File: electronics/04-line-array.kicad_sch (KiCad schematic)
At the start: 54 parts, among them Q401 AO3400A, Q402 AO3400A, U401 ITR8307/S17/TR8, U402 ITR8307/S17/TR8, U403 ITR8307/S17/TR8, U404 ITR8307/S17/TR8, U405 ITR8307/S17/TR8, U406 ITR8307/S17/TR8, U407 ITR8307/S17/TR8, U408 ITR8307/S17/TR8, U409 ITR8307/S17/TR8, U410 ITR8307/S17/TR8, U411 ITR8307/S17/TR8, U412 ITR8307/S17/TR8

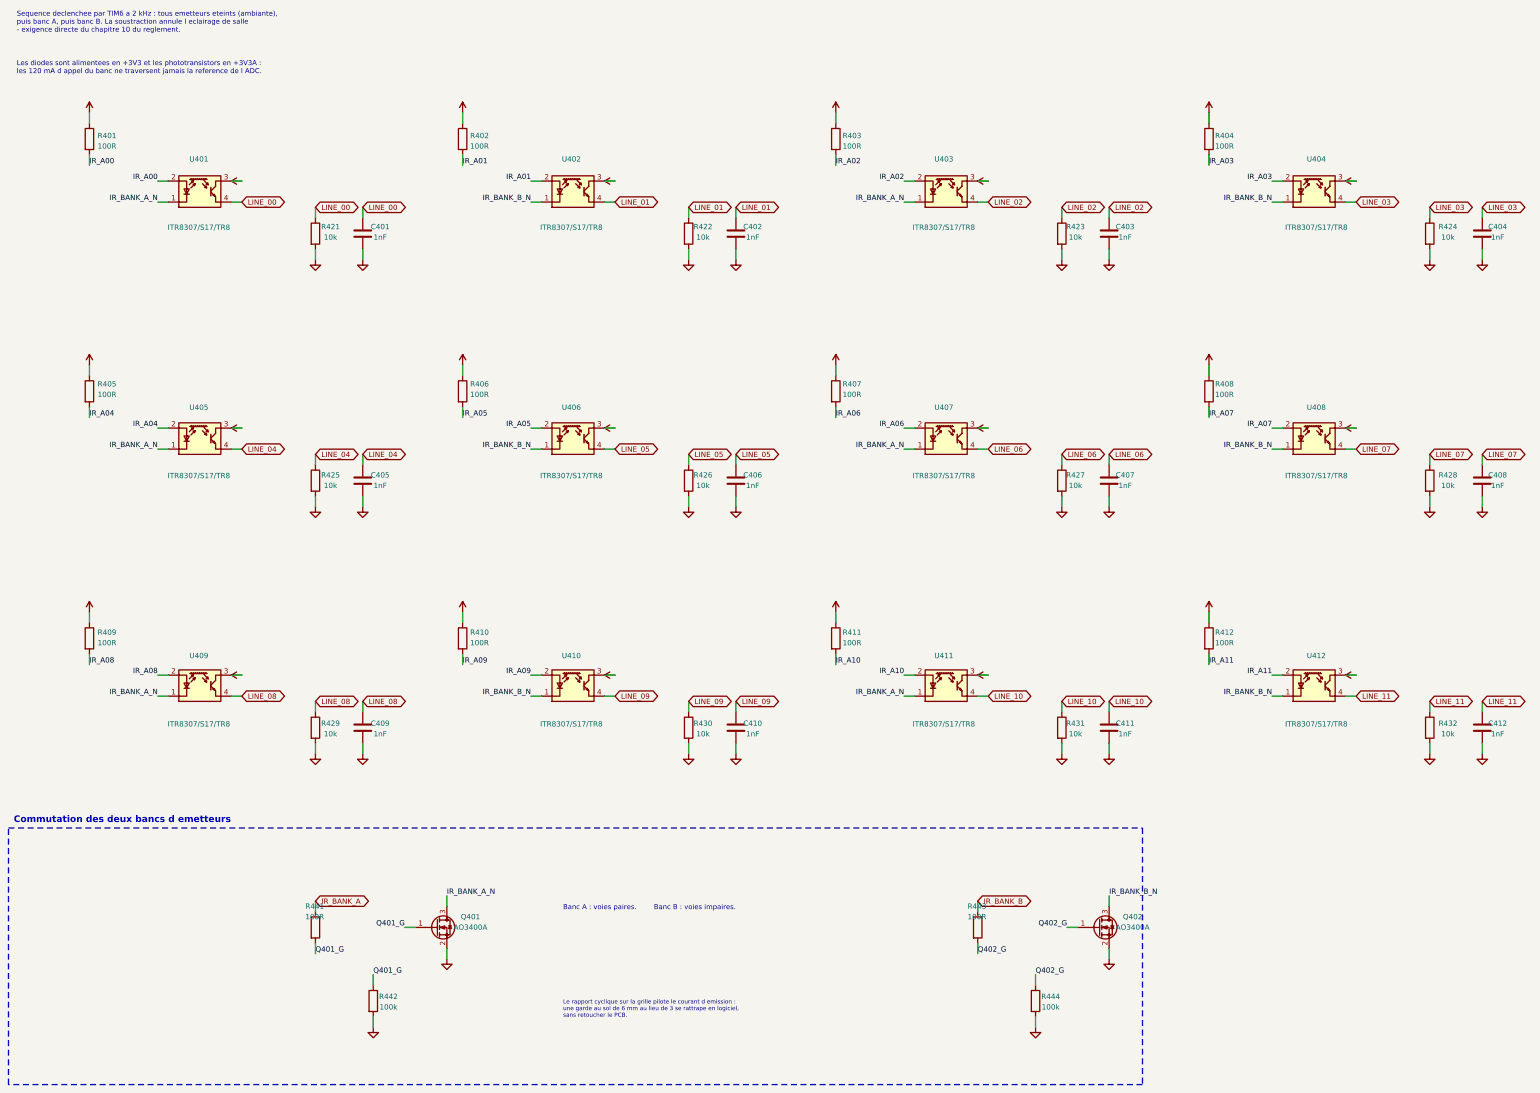
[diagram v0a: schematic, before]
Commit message: Passe le microcontrôleur en LQFP144 et lit les deux courants au même instant
Le LQFP100 avait ses seize entrées ADC prises — douze voies de ligne, trois
de télémétrie, une sortie de multiplexeur — et c'est ce multiplexeur qui
posait le vrai problème : il interdisait par construction de lire les deux
courants moteur ensemble. On lisait un moteur, on commutait, on attendait
l'établissement, on lisait l'autre. Le STM32H723ZGT6 en LQFP144 place
PF11 sur ADC1_INP2 et PF13 sur ADC2_INP2 : même numéro de voie sur deux
convertisseurs, donc une lecture simultanée en mode double, et le 74HC4051
disparaît de la carte.

Le brochage étant donné par nom de port et non par numéro de broche, le
passage a coûté deux affectations sur quatre-vingt-sept. Une affectation est
un choix de port — PA0 porte la voie de ligne 00 — jamais un choix de patte.
Une table numérotée aurait demandé de recopier 144 lignes à la main, et une
erreur de brochage ne se voit pas à l'ERC.

Ajoute une huitième feuille, les témoins de ligne. Ce qu'on regarde pendant
un essai n'est pas un témoin d'état générique, c'est ce que voit la
moustache : une LED par capteur, à l'aplomb du capteur qu'elle rapporte, et
un capteur borgne se voit avant la course plutôt qu'après. Le rapport
cyclique suit le signal, sinon rien ne dirait si la ligne est au bord ou au
centre du trait. PCA9685 à l'adresse 0x40 sur I²C2, 52 octets par rafale
soit 1,2 ms à 400 kHz, en DMA hors de la boucle rapide.

Remplace l'interrupteur à glissière par une mise sous tension à bouton
poussoir : une impulsion amorce, le microcontrôleur se tient lui-même, et
c'est lui qui coupe. La glissière demandait une place au bord de carte que
le pack, l'équilibrage et les fils de l'ESC ont fini par prendre — et elle
ne savait pas éteindre proprement, couper le 3,3 V sous les pieds du
firmware n'ayant jamais rien écrit dans la flash.

Ajoute au générateur le contrôle qui manquait : deux extrémités de nets
différents au même point. Il a fallu qu'il relie B+ à B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
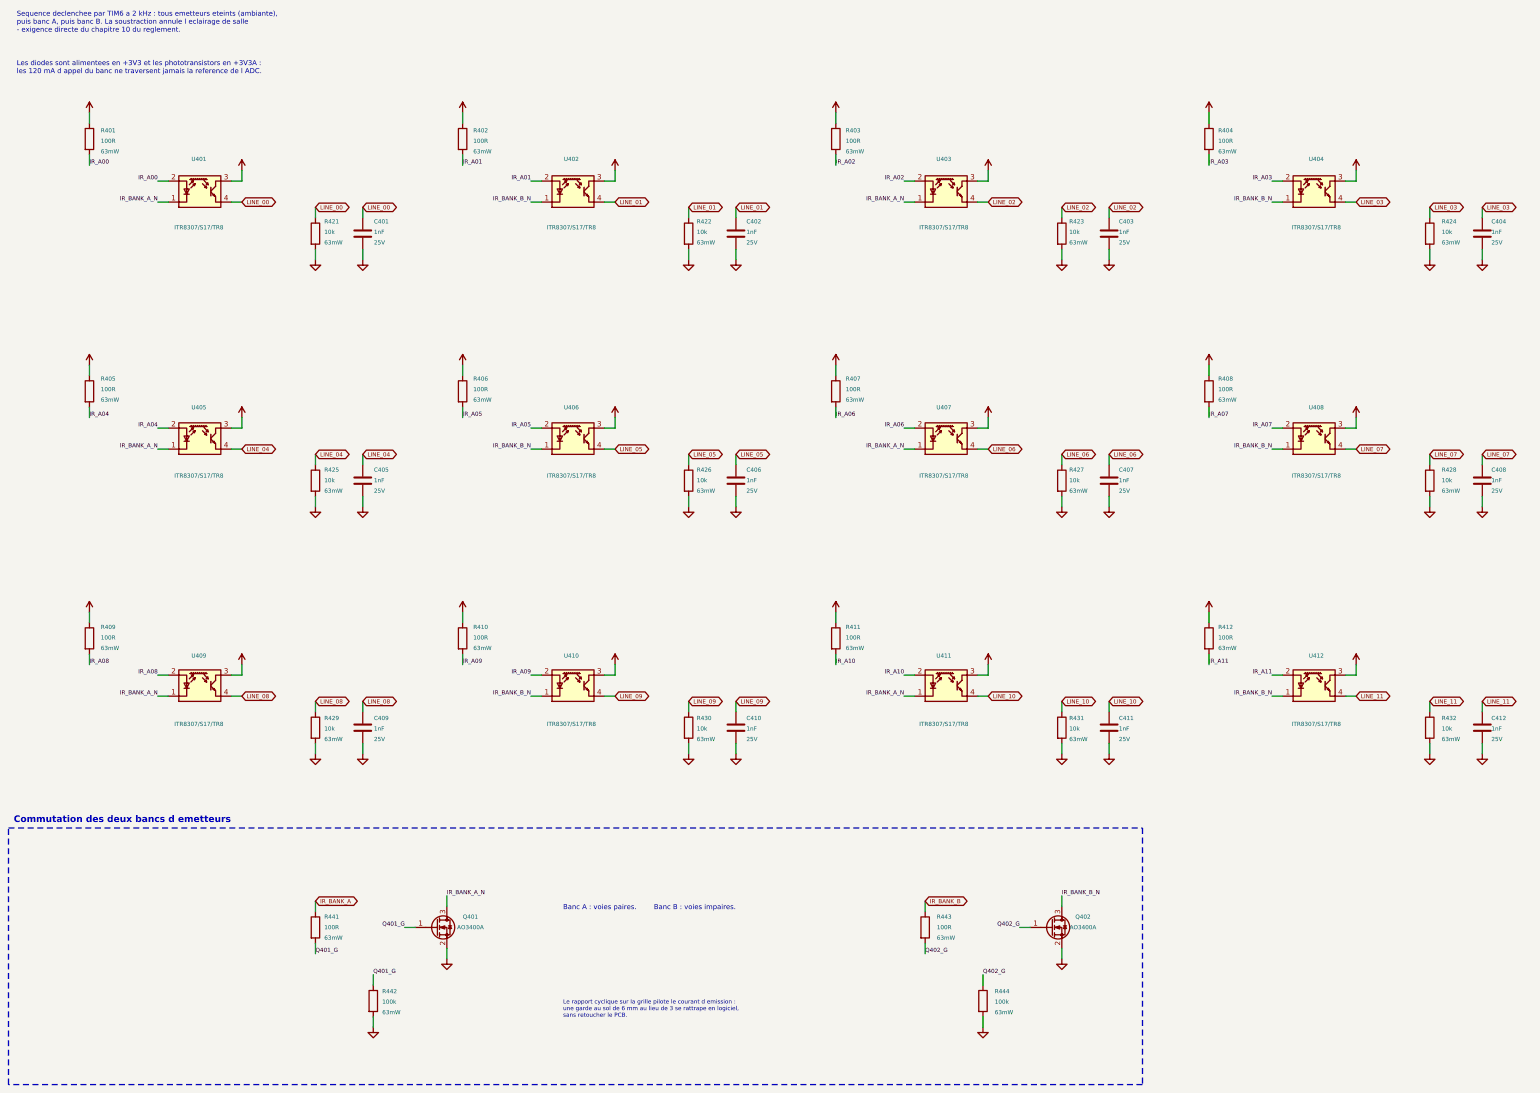
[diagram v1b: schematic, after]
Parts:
- C401, C402, C403, C404, C405, C406, C407, C408, C409, C410, C411, C412: footprint Capacitor_SMD:C_0603_1608Metric -> Capacitor_SMD:C_0402_1005Metric; Dielectric (none) -> X7R; Voltage (none) -> 25V
- R401, R402, R403, R404, R405, R406, R407, R408, R409, R410, R411, R412, R421, R422, R423, R424, R425, R426, R427, R428, R429, R430, R431, R432, R441, R442, R443, R444: footprint Resistor_SMD:R_0603_1608Metric -> Resistor_SMD:R_0402_1005Metric; Power (none) -> 63mW
- U401, U402, U403, U404, U405, U406, U407, U408, U409, U410, U411, U412: footprint OptoDevice:Everlight_ITR8307 -> Pacabot:ITR8307_dessous
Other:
- moved on the sheet: Q402, R443, R444

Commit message: Replace la carte autour de ses chaînes analogiques et y intègre le pack commun et l'ESC
Le placement du 4 septembre rangeait les pièces par zone. Celui-ci part des
nets et des vraies pastilles, et affecte chaque condensateur à une broche
plutôt qu'à une couronne autour du boîtier. Le STM32 pivote de 180° sur son
centre pour tourner son côté analogique vers la barrette. Chaque station
laser reçoit son propre TLV9064 (U504 s'ajoute pour la station L), et la
liaison photodiode → TIA tombe de 34, 56 et 69 mm à 3,1, 7,4 et 2,9 mm. La
boucle de retour du TIA passe de 140–150 mm à 3,55. Cinq découplages
suivent : C568, C569/C570 sur VREF_RX, C223/C224 sur VBAT du MCU et C351
sur VREF_MOT du pont droit.

`layout.py`, `layout_fit.json` et `place_pcb.py --reset` ne décrivent plus
cette carte. Le README le dit en tête, et les nouveaux outils partent du
PCB courant, jamais de l'ancienne table. `audit_placement_geometry.py` relit
les courtyards orientés et les contrôle sous Shapely, `placement_metrics.py`
et `preview_analog_paths.py` mesurent distances et couloirs sans poser une
piste. `refine_placement.py` calcule la table, `apply_refined_placement.py`
l'écrit en vérifiant verrous et UUID : il ne se rejoue pas après une
retouche à la main.

L'alimentation change de nature. Le pack LiFePO4 et son ESC sur VBAT
laissent place à un pack 2S commun, chimie encore à choisir, que la carte,
les moteurs et la turbine partagent. Une seule prise MR30 à trois contacts
porte GND, point milieu et VPACK, et remplace XT30 + JST-XH. L'ESC devient
un EMAX Bullet 12A (12 A continu, 15 A crête, sans BEC) sur VPACK brut,
monté debout sur J103. J104 et J702 disparaissent. ESC103 et M703 sont des
symboles hors carte : les phases moteur ne reçoivent aucun pad fictif, et
le module ne compte qu'une fois dans la nomenclature. R107 passe de 10 à
47 Ω pour ramener l'équilibrage à 88 mA et 0,36 W, sous le watt de son
boîtier 2512. La recharge reste inhibée par défaut matériel tant que
cellules, profil et fir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
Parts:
- U401, U402, U403, U404, U405, U406, U407, U408, U409, U410, U411, U412: value ITR8307/S17/TR8 -> ITR8307/S17/TR8(B); footprint Pacabot:ITR8307_dessous -> Pacabot:ITR8307_S17_TR8_Bottom
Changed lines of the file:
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@@
 			)
 		)
-		(property "Value" "ITR8307/S17/TR8"
+		(property "Value" "ITR8307/S17/TR8(B)"
 			(at 62 70.89 0)
 			(effects
@@
 			)
 		)
-		(property "Footprint" "Pacabot:ITR8307_dessous"
+		(property "Footprint" "Pacabot:ITR8307_S17_TR8_Bottom"
 			(at 62.23 62.23 0)
 			(effects
@@
 			)
 		)
-		(property "Datasheet" "~"
+		(property "Datasheet" "https://www.everlighteurope.com/custom/files/datasheets/DRX-0000322.pdf"
 			(at 62.23 62.23 0)
 			(effects
@@
 			)
 		)
-		(property "Value" "ITR8307/S17/TR8"
+		(property "Value" "ITR8307/S17/TR8(B)"
 			(at 152 70.89 0)
 			(effects
@@
 			)
 		)
-		(property "Footprint" "Pacabot:ITR8307_dessous"
+		(property "Footprint" "Pacabot:ITR8307_S17_TR8_Bottom"
 			(at 152.4 62.23 0)
 			(effects
@@
 			)
 		)
-		(property "Datasheet" "~"
+		(property "Datasheet" "https://www.everlighteurope.com/custom/files/datasheets/DRX-0000322.pdf"
 			(at 152.4 62.23 0)
 			(effects
@@
 			)
 		)
-		(property "Value" "ITR8307/S17/TR8"
+		(property "Value" "ITR8307/S17/TR8(B)"
 			(at 242 70.89 0)
 			(effects
@@
 			)
 		)
-		(property "Footprint" "Pacabot:ITR8307_dessous"
+		(property "Footprint" "Pacabot:ITR8307_S17_TR8_Bottom"
 			(at 242.57 62.23 0)
 			(effects
@@
 			)
 		)
-		(property "Datasheet" "~"
+		(property "Datasheet" "https://www.everlighteurope.com/custom/files/datasheets/DRX-0000322.pdf"
 			(at 242.57 62.23 0)
 			(effects
@@
 			)
 		)
-		(property "Value" "ITR8307/S17/TR8"
+		(property "Value" "ITR8307/S17/TR8(B)"
 			(at 332 70.89 0)
 			(effects
@@
 			)
 		)
-		(property "Footprint" "Pacabot:ITR8307_dessous"
+		(property "Footprint" "Pacabot:ITR8307_S17_TR8_Bottom"
 			(at 331.47 62.23 0)
 			(effects
@@
 			)
 		)
-		(property "Datasheet" "~"
+		(property "Datasheet" "https://www.everlighteurope.com/custom/files/datasheets/DRX-0000322.pdf"
 			(at 331.47 62.23 0)
 			(effects
@@
 			)
 		)
-		(property "Value" "ITR8307/S17/TR8"
+		(property "Value" "ITR8307/S17/TR8(B)"
 			(at 62 130.89 0)
 			(effects
@@
 			)
 		)
-		(property "Footprint" "Pacabot:ITR8307_dessous"
+		(property "Footprint" "Pacabot:ITR8307_S17_TR8_Bottom"
 			(at 62.23 121.92 0)
 			(effects
@@
 			)
 		)
-		(property "Datasheet" "~"
+		(property "Datasheet" "https://www.everlighteurope.com/custom/files/datasheets/DRX-0000322.pdf"
 			(at 62.23 121.92 0)
 			(effects
@@
 			)
 		)
-		(property "Value" "ITR8307/S17/TR8"
+		(property "Value" "ITR8307/S17/TR8(B)"
 			(at 152 130.89 0)
 			(effects
@@
 			)
 		)
-		(property "Footprint" "Pacabot:ITR8307_dessous"
+		(property "Footprint" "Pacabot:ITR8307_S17_TR8_Bottom"
 			(at 152.4 121.92 0)
 			(effects
@@
 			)
 		)
-		(property "Datasheet" "~"
+		(property "Datasheet" "https://www.everlighteurope.com/custom/files/datasheets/DRX-0000322.pdf"
 			(at 152.4 121.92 0)
 			(effects
@@
 			)
 		)
-		(property "Value" "ITR8307/S17/TR8"
+		(property "Value" "ITR8307/S17/TR8(B)"
 			(at 242 130.89 0)
 			(effects
@@
 			)
 		)
-		(property "Footprint" "Pacabot:ITR8307_dessous"
+		(property "Footprint" "Pacabot:ITR8307_S17_TR8_Bottom"
 			(at 242.57 121.92 0)
 			(effects
@@
 			)
 		)
-		(property "Datasheet" "~"
+		(property "Datasheet" "https://www.everlighteurope.com/custom/files/datasheets/DRX-0000322.pdf"
 			(at 242.57 121.92 0)
 			(effects
@@
 			)
 		)
-		(property "Value" "ITR8307/S17/TR8"
+		(property "Value" "ITR8307/S17/TR8(B)"
 			(at 332 130.89 0)
 			(effects
@@
 			)
 		)
-		(property "Footprint" "Pacabot:ITR8307_dessous"
+		(property "Footprint" "Pacabot:ITR8307_S17_TR8_Bottom"
 			(at 331.47 121.92 0)
 			(effects
@@
 			)
 		)
-		(property "Datasheet" "~"
+		(property "Datasheet" "https://www.everlighteurope.com/custom/files/datasheets/DRX-0000322.pdf"
 			(at 331.47 121.92 0)
 			(effects
@@
 			)
 		)
-		(property "Value" "ITR8307/S17/TR8"
+		(property "Value" "ITR8307/S17/TR8(B)"
 			(at 62 190.89 0)
 			(effects
@@
 			)
 		)
-		(property "Footprint" "Pacabot:ITR8307_dessous"
+		(property "Footprint" "Pacabot:ITR8307_S17_TR8_Bottom"
 			(at 62.23 181.61 0)
 			(effects
@@
 			)
 		)
-		(property "Datasheet" "~"
+		(property "Datasheet" "https://www.everlighteurope.com/custom/files/datasheets/DRX-0000322.pdf"
 			(at 62.23 181.61 0)
 			(effects
@@
 			)
 		)
-		(property "Value" "ITR8307/S17/TR8"
+		(property "Value" "ITR8307/S17/TR8(B)"
 			(at 152 190.89 0)
 			(effects
@@
 			)
 		)
-		(property "Footprint" "Pacabot:ITR8307_dessous"
+		(property "Footprint" "Pacabot:ITR8307_S17_TR8_Bottom"
 			(at 152.4 181.61 0)
 			(effects
@@
 			)
 		)
-		(property "Datasheet" "~"
+		(property "Datasheet" "https://www.everlighteurope.com/custom/files/datasheets/DRX-0000322.pdf"
 			(at 152.4 181.61 0)
 			(effects
@@
 			)
 		)
-		(property "Value" "ITR8307/S17/TR8"
+		(property "Value" "ITR8307/S17/TR8(B)"
 			(at 242 190.89 0)
 			(effects
@@
 			)
 		)
-		(property "Footprint" "Pacabot:ITR8307_dessous"
+		(property "Footprint" "Pacabot:ITR8307_S17_TR8_Bottom"
 			(at 242.57 181.61 0)
 			(effects
@@
 			)
 		)
-		(property "Datasheet" "~"
+		(property "Datasheet" "https://www.everlighteurope.com/custom/files/datasheets/DRX-0000322.pdf"
 			(at 242.57 181.61 0)
 			(effects
@@
 			)
 		)
-		(property "Value" "ITR8307/S17/TR8"
+		(property "Value" "ITR8307/S17/TR8(B)"
 			(at 332 190.89 0)
 			(effects
@@
 			)
 		)
-		(property "Footprint" "Pacabot:ITR8307_dessous"
+		(property "Footprint" "Pacabot:ITR8307_S17_TR8_Bottom"
 			(at 331.47 181.61 0)
 			(effects
@@
 			)
 		)
-		(property "Datasheet" "~"
+		(property "Datasheet" "https://www.everlighteurope.com/custom/files/datasheets/DRX-0000322.pdf"
 			(at 331.47 181.61 0)
 			(effects
